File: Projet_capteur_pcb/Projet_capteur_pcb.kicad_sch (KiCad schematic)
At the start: 18 parts, among them J1 Power, J2 Digital/PWM, J3 Analog, J4 Digital/PWM

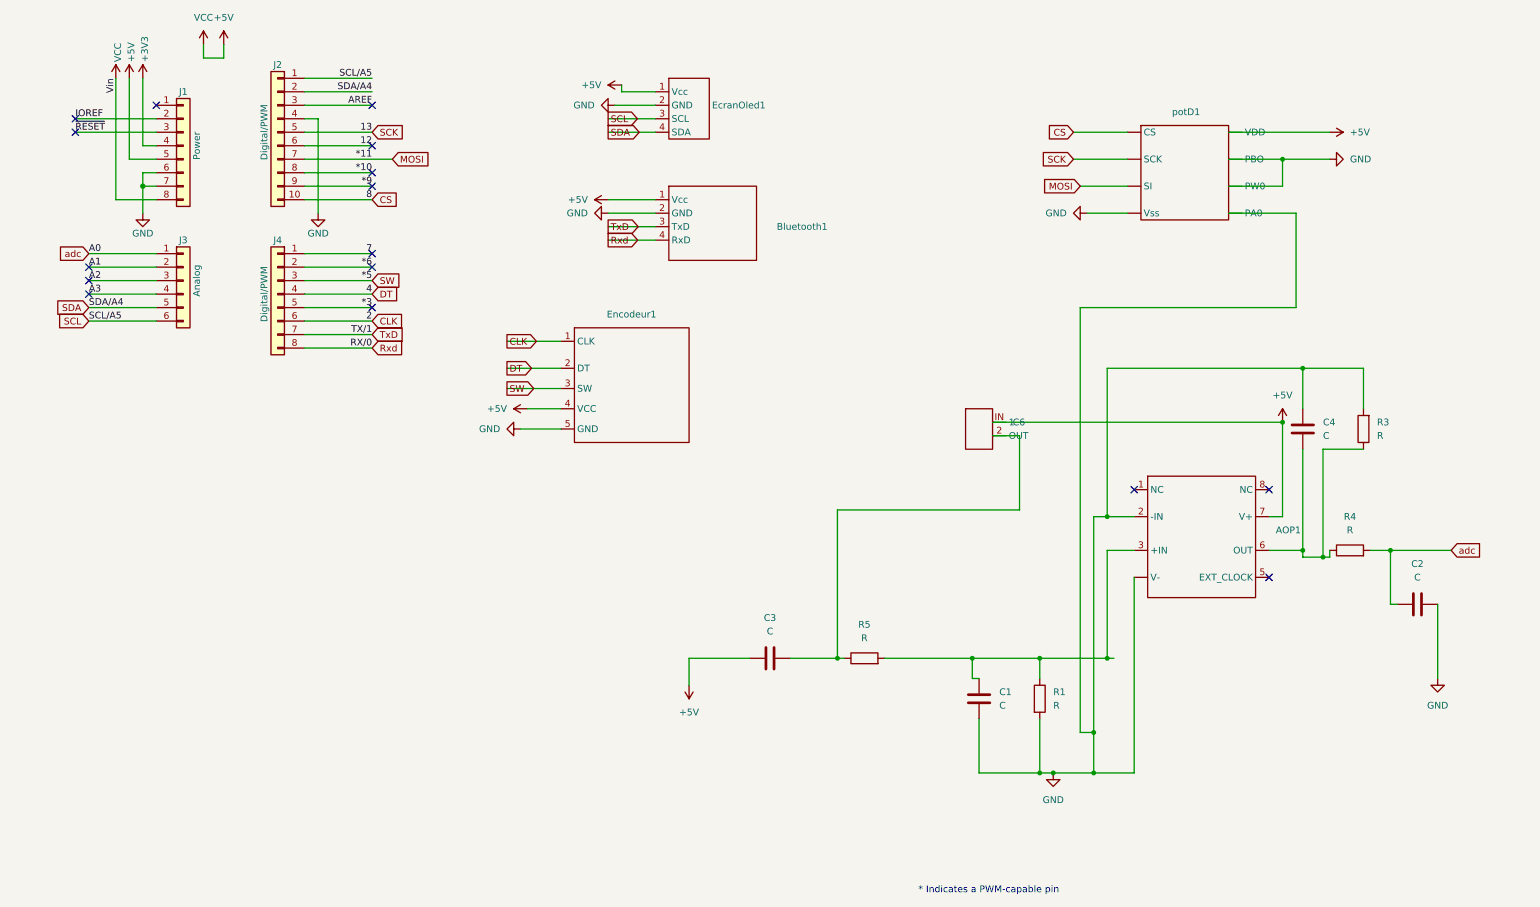
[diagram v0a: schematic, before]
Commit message: changement pin
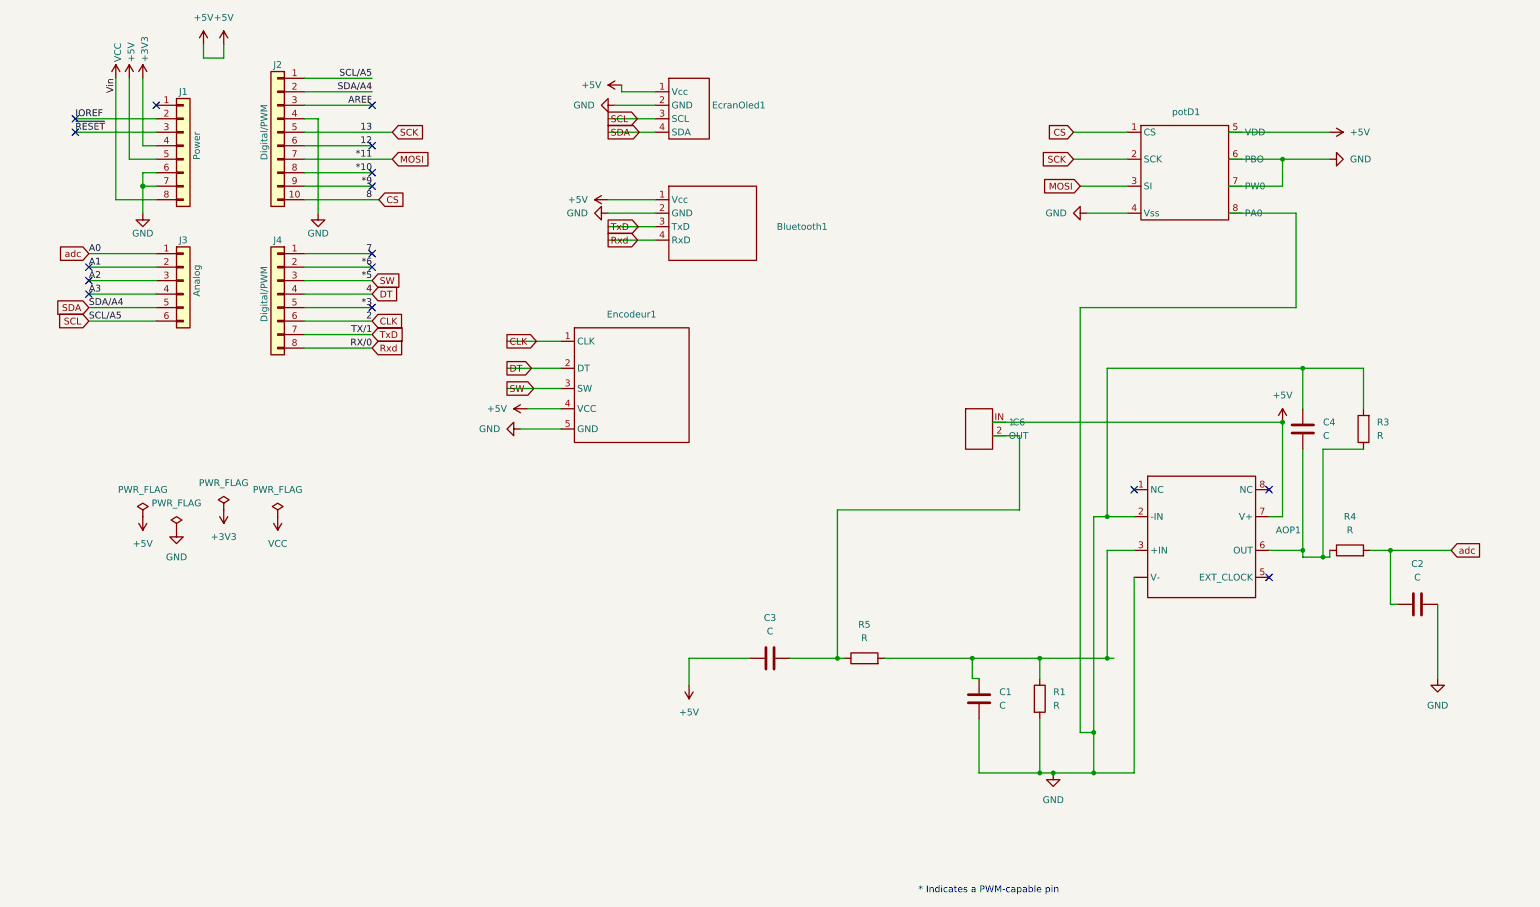
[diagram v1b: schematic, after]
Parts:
- AOP1: footprint Librairie_empreinte:DIP-8_296_ELL -> Librairie_empreinte:AO
- Bluetooth1: footprint Librairie_empreinte:SIP-4 -> Librairie_empreinte:Empreinte_bluetooth
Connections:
- net +5V: now also potD1.5 (VDD); no longer J1.8 (Pin_8), potD1. (PA0)
- net CS: now also potD1.1 (CS); no longer potD1. (PA0)
- net GND: now also potD1.4 (Vss), potD1.6 (PBO), potD1.7 (PW0), potD1.8 (PA0); no longer potD1. (PA0)
- net MOSI: now also potD1.3 (SI); no longer potD1. (PA0)
- net SCK: now also potD1.2 (SCK); no longer potD1. (PA0)
- new net VCC: J1.8 (Pin_8)

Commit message: routage
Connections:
- net +5V: now also C6.1 (IN); no longer C6.IN (1)
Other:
- moved on the sheet: AOP1
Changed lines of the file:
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@@
 	)
 	(junction
-		(at 213.36 135.89)
-		(diameter 0)
-		(color 0 0 0 0)
-	)
-	(junction
-		(at 213.36 109.22)
+		(at 250.19 109.22)
 		(diameter 0)
 		(color 0 0 0 0)
@@
 	)
 	(junction
-		(at 200.66 135.89)
-		(diameter 0)
-		(color 0 0 0 0)
-	)
-	(junction
 		(at 266.7 115.57)
 		(diameter 0)
@@
 	)
 	(junction
-		(at 250.19 115.57)
+		(at 200.66 135.89)
+		(diameter 0)
+		(color 0 0 0 0)
+	)
+	(junction
+		(at 213.36 101.6)
 		(diameter 0)
 		(color 0 0 0 0)
@@
 	)
 	(no_connect
-		(at 243.84 120.65)
+		(at 241.3 114.3)
 	)
 	(no_connect
-		(at 218.44 104.14)
+		(at 215.9 97.79)
 	)
 	(no_connect
@@
 	)
 	(no_connect
-		(at 243.84 104.14)
+		(at 241.3 97.79)
 	)
 	(no_connect
@@
 	(wire
 		(pts
-			(xy 243.84 115.57) (xy 250.19 115.57)
+			(xy 241.3 109.22) (xy 250.19 109.22)
 		)
 		(stroke
@@
 	(wire
 		(pts
-			(xy 213.36 135.89) (xy 214.63 135.89)
+			(xy 31.75 44.45) (xy 31.75 46.99)
 		)
 		(stroke
 			(width 0)
-			(type default)
+			(type solid)
 		)
 	)
 	(wire
 		(pts
-			(xy 31.75 44.45) (xy 31.75 46.99)
+			(xy 213.36 81.28) (xy 213.36 101.6)
 		)
 		(stroke
 			(width 0)
-			(type solid)
+			(type default)
 		)
 	)
@@
 	(wire
 		(pts
-			(xy 243.84 109.22) (xy 246.38 109.22)
+			(xy 210.82 101.6) (xy 213.36 101.6)
+		)
+		(stroke
+			(width 0)
+			(type default)
+		)
+	)
+	(wire
+		(pts
+			(xy 241.3 102.87) (xy 246.38 102.87)
 		)
 		(stroke
@@
 	(wire
 		(pts
-			(xy 210.82 157.48) (xy 218.44 157.48)
+			(xy 215.9 157.48) (xy 210.82 157.48)
 		)
 		(stroke
@@
 	(wire
 		(pts
-			(xy 213.36 115.57) (xy 218.44 115.57)
+			(xy 200.66 109.22) (xy 215.9 109.22)
 		)
 		(stroke
@@
 	(wire
 		(pts
-			(xy 250.19 96.52) (xy 250.19 115.57)
+			(xy 250.19 96.52) (xy 250.19 109.22)
 		)
 		(stroke
@@
 	(wire
 		(pts
-			(xy 213.36 109.22) (xy 218.44 109.22)
+			(xy 213.36 102.87) (xy 215.9 102.87)
 		)
 		(stroke
@@
 	(wire
 		(pts
-			(xy 213.36 109.22) (xy 213.36 81.28)
-		)
-		(stroke
-			(width 0)
-			(type default)
-		)
-	)
-	(wire
-		(pts
 			(xy 62.23 67.31) (xy 74.93 67.31)
 		)
@@
 	(wire
 		(pts
-			(xy 246.38 91.44) (xy 246.38 109.22)
+			(xy 246.38 91.44) (xy 246.38 102.87)
 		)
 		(stroke
@@
 	(wire
 		(pts
-			(xy 19.05 34.29) (xy 34.29 34.29)
+			(xy 213.36 101.6) (xy 213.36 102.87)
 		)
 		(stroke
 			(width 0)
-			(type solid)
+			(type default)
 		)
 	)
 	(wire
 		(pts
-			(xy 213.36 115.57) (xy 213.36 135.89)
+			(xy 19.05 34.29) (xy 34.29 34.29)
 		)
 		(stroke
 			(width 0)
-			(type default)
+			(type solid)
 		)
 	)
@@
 	(wire
 		(pts
-			(xy 34.29 46.99) (xy 31.75 46.99)
+			(xy 200.66 135.89) (xy 200.66 109.22)
 		)
 		(stroke
 			(width 0)
-			(type solid)
+			(type default)
 		)
 	)
 	(wire
 		(pts
-			(xy 248.92 69.85) (xy 248.92 52.07)
+			(xy 34.29 46.99) (xy 31.75 46.99)
 		)
 		(stroke
 			(width 0)
-			(type default)
+			(type solid)
 		)
 	)
 	(wire
 		(pts
-			(xy 210.82 109.22) (xy 213.36 109.22)
+			(xy 248.92 69.85) (xy 248.92 52.07)
 		)
 		(stroke
@@
 	(wire
 		(pts
-			(xy 200.66 135.89) (xy 213.36 135.89)
+			(xy 250.19 109.22) (xy 250.19 116.84)
 		)
 		(stroke
@@
 	(wire
 		(pts
-			(xy 250.19 115.57) (xy 250.19 116.84)
-		)
-		(stroke
-			(width 0)
-			(type default)
-		)
-	)
-	(wire
-		(pts
 			(xy 21.59 59.69) (xy 34.29 59.69)
 		)
@@
 	(wire
 		(pts
-			(xy 218.44 120.65) (xy 218.44 157.48)
+			(xy 215.9 114.3) (xy 215.9 157.48)
 		)
 		(stroke
@@
 	(wire
 		(pts
-			(xy 210.82 109.22) (xy 210.82 149.86)
+			(xy 210.82 101.6) (xy 210.82 149.86)
 		)
 		(stroke
@@
 	(symbol
 		(lib_id "Graphique_bluetooth:aop")
-		(at 231.14 113.03 0)
+		(at 228.6 106.68 0)
 		(unit 1)
 		(exclude_from_sim no)
@@
 		(fields_autoplaced yes)
 		(property "Reference" "AOP1"
-			(at 245.11 111.7599 0)
+			(at 242.57 105.4099 0)
 			(effects
 				(font
@@
 		)
 		(property "Value" "~"
-			(at 245.11 114.2999 0)
+			(at 242.57 107.9499 0)
 			(effects
 				(font
@@
 		)
 		(property "Footprint" "Librairie_empreinte:AO"
-			(at 231.14 113.03 0)
+			(at 228.6 106.68 0)
 			(effects
 				(font
@@
 		)
 		(property "Datasheet" ""
-			(at 231.14 113.03 0)
+			(at 228.6 106.68 0)
 			(effects
 				(font
@@
 		)
 		(property "Description" ""
-			(at 231.14 113.03 0)
+			(at 228.6 106.68 0)
 			(effects
 				(font
@@
 				)
 				(justify left)
+				(hide yes)
 			)
 		)
@@
 			)
 		)
-		(pin "IN"
+		(pin "1"
 		)
 		(pin "2"

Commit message: routage V1
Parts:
- removed C3: C, Capacitor_THT:C_Disc_D7.5mm_W2.5mm_P5.00mm, symbol Device:C
- C1, C2: value C -> 100n
- C4: value C -> 1u
- R1, R3: value R -> 100k
- R4: value R -> 1k
- R5: value R -> 10K
- capteur1: renamed from C6; footprint (none) -> Librairie_empreinte:DIP-2_296_ELL
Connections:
- net GND: now also AOP1.4 (V-); no longer AOP1. (V-), AOP1.2 (-IN), C4.1, R3.2, potD1.8 (PA0)
- net A1 renamed flex_out
- net adc renamed ampli_out
- new net potor_out: AOP1.2 (-IN), C4.1, R3.2, potD1.8 (PA0)
- no-connect marks 16 -> 15
